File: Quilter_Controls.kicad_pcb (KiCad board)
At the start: 2 copper layers, 50.6 x 110 mm, 16 parts, among them J1 Conn_01x10_Male, J10 Conn_01x04_Male, J2 Conn_01x10_Male, J3 Conn_01x10_Male, J4 Audio_In, J5 Audio_Out, J6 Audio_Mix, J7 Freq_V_Oct, J8 Freq_CV, J9 Conn_02x04_Top_Bottom

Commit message: First draft routing of Controls PCB
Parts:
- J1, J2: moved to B.Cu
- moved TP1 91.0 mm to (53.7, 55.5)
- moved TP3 80.7 mm to (70.2, 43.0)
- moved J9 72.7 mm to (60.6, 43.8), turned to -90 degrees
- moved TP4 64.7 mm to (86.9, 147.0)
- moved TP2 62.9 mm to (86.6, 55.5)
- moved J10 40.9 mm to (87.8, 43.7), turned to -90 degrees
- moved J8 14.2 mm to (80.0, 100.9)
- moved J5 13.5 mm to (80.0, 121.3)
- moved J1 11.4 mm to (87.9, 62.8), turned to 180 degrees
- moved J7 10.1 mm to (60.4, 100.9)
- moved J6 9.27 mm to (70.2, 138.9), turned to 180 degrees
- moved J4 9.12 mm to (60.4, 121.3)
- moved J3 8.88 mm to (81.7, 147.9)
- moved Q_CTRL1 7.91 mm to (70.2, 79.2)
- moved FREQ_POT1 7.91 mm to (70.2, 55.5)
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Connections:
- J1 pad 1: unconnected-(J1-Pad1) -> -12V
- J1 pad 3: unconnected-(J1-Pad3) -> /AUDIO_BUFF3
- J1 pad 7: unconnected-(J1-Pad7) -> /FREQ_V_OCT2
- J1 pad 8: /AUDIO_BUFF4 -> unconnected-(J1-Pad8)
- J2 pad 1: unconnected-(J2-Pad1) -> +12V
- J2 pad 10: /FREQ_POT_5V -> /AUDIO_IN2
- J2 pad 2: /AUDIO_BUFF3 -> unconnected-(J2-Pad2)
- J2 pad 4: /FREQ_V_OCT2 -> unconnected-(J2-Pad4)
- J2 pad 5: unconnected-(J2-Pad5) -> /AUDIO_BUFF4
- J2 pad 7: unconnected-(J2-Pad7) -> /FREQ_POT_5V
- J2 pad 9: /AUDIO_IN2 -> unconnected-(J2-Pad9)
- J3 pad 1: unconnected-(J3-Pad1) -> /AUDIO_IN4
- J3 pad 3: /FREQ_CV4 -> unconnected-(J3-Pad3)
- J3 pad 5: /AUDIO_IN4 -> /FREQ_POT
- J3 pad 6: /FREQ_CV1 -> /FREQ_CV4
- J3 pad 7: /FREQ_POT -> /FREQ_CV1
- J9 pad 2: /AUDIO_IN2 -> /FREQ_V_OCT1
- J9 pad 3: /AUDIO_IN3 -> /AUDIO_IN2
- J9 pad 4: /AUDIO_IN4 -> /FREQ_V_OCT2
- J9 pad 5: /FREQ_V_OCT1 -> /AUDIO_IN3
- J9 pad 6: /FREQ_V_OCT2 -> /FREQ_V_OCT3
- J9 pad 7: /FREQ_V_OCT3 -> /AUDIO_IN4
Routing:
- net /AUDIO_IN4: track 0.00 -> 156.8 mm
- net /FREQ_V_OCT3: track 0.00 -> 142.3 mm
- net /FREQ_V_OCT4: track 0.00 -> 126.1 mm
- net /AUDIO_IN3: track 0.00 -> 125.1 mm
- net /AUDIO_BUFF2: track 0.00 -> 115.0 mm
- net /AUDIO_IN1: track 0.00 -> 112.0 mm, vias 0 -> 1
- net /FREQ_POT: track 0.00 -> 111.0 mm, vias 0 -> 1
- net /FREQ_V_OCT2: track 0.00 -> 109.0 mm
- net /FREQ_V_OCT1: track 0.00 -> 108.9 mm
- net /AUDIO_BUFF4: track 0.00 -> 100.2 mm
- net /AUDIO_BUFF1: track 0.00 -> 92.3 mm
- net /AUDIO_MIX: track 0.00 -> 91.3 mm
- net /Q_POT: track 0.00 -> 82.2 mm, vias 0 -> 1
- net /AUDIO_BUFF3: track 0.00 -> 81.8 mm
- net /AUDIO_IN2: track 0.00 -> 79.6 mm
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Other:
- board size 50.6 x 110 mm -> 40.4 x 110 mm

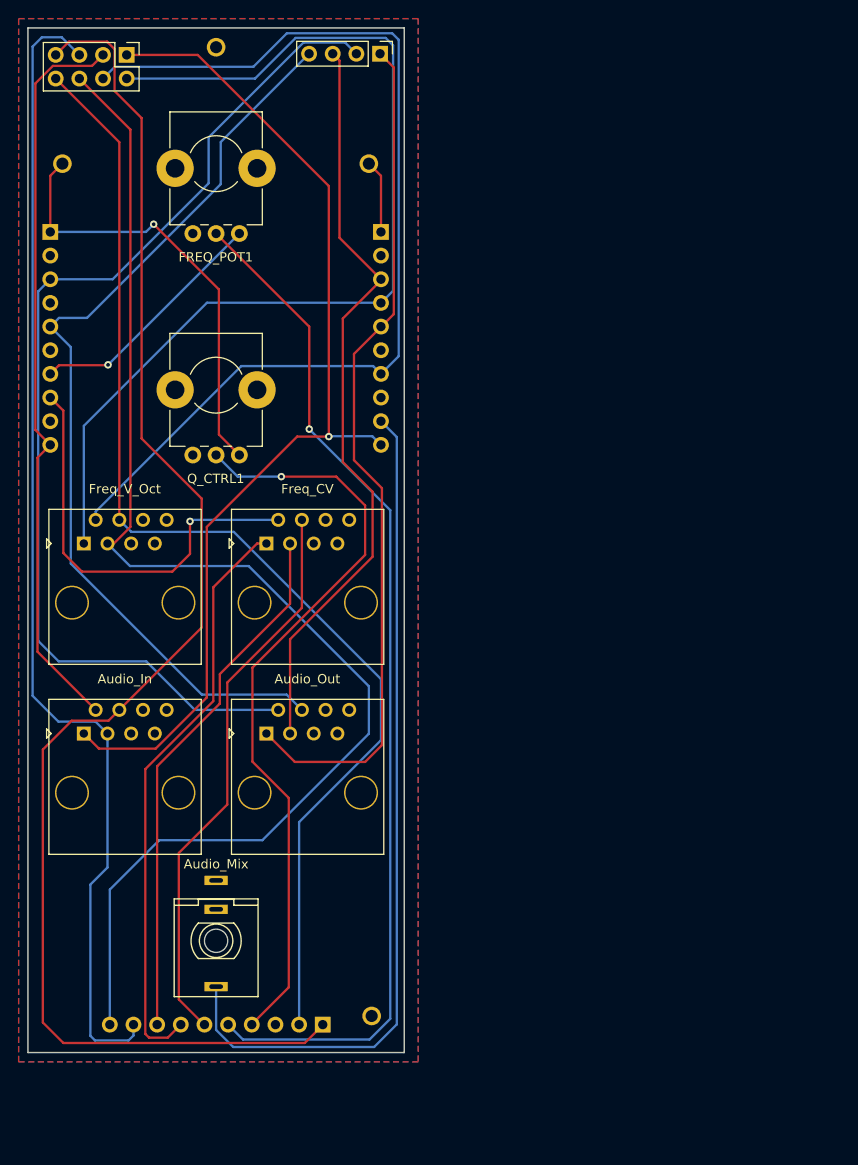
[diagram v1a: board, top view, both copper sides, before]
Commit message: Fixed orientation of connector headers
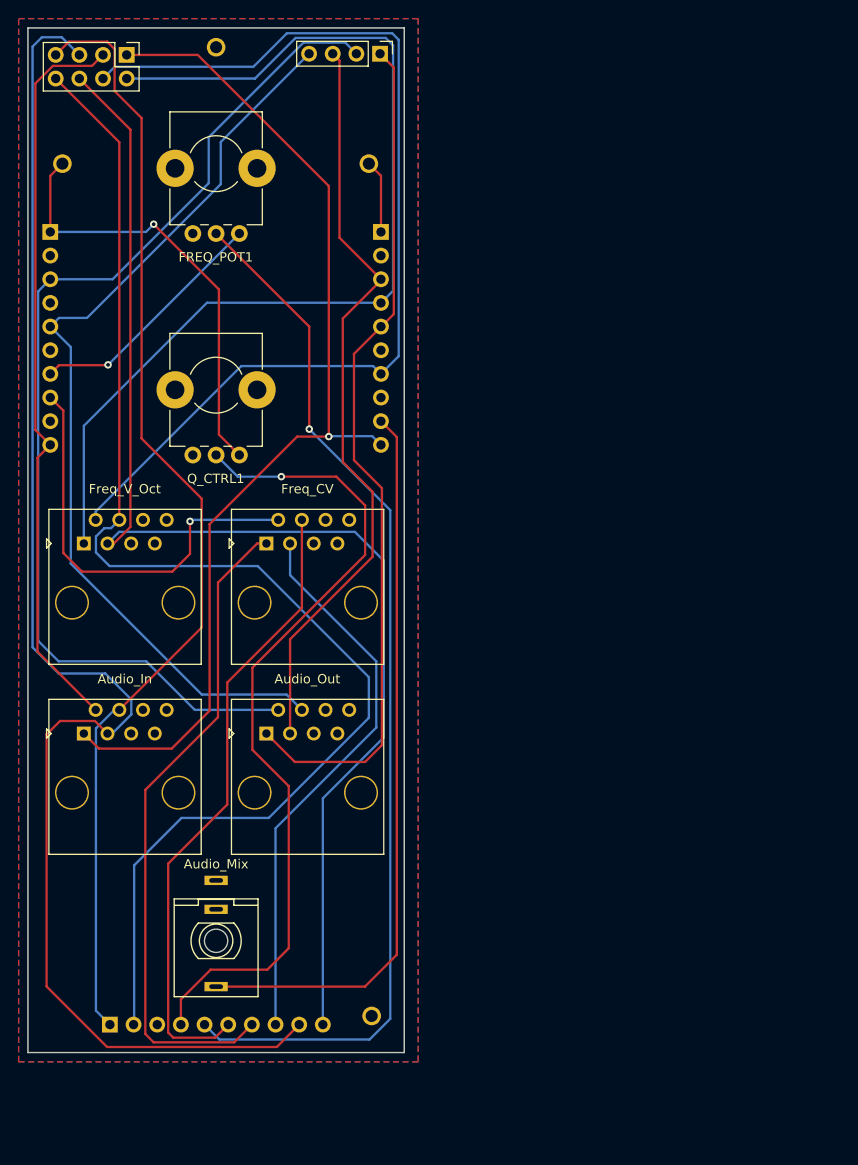
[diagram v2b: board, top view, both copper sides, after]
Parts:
- moved J3 22.9 mm to (58.8, 147.9), turned to -90 degrees
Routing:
- net /AUDIO_IN4: track 156.8 -> 121.5 mm
- net /AUDIO_IN3: track 125.1 -> 154.2 mm
- net /FREQ_V_OCT4: track 126.1 -> 143.3 mm
- net /AUDIO_MIX: track 91.3 -> 78.8 mm
- net /FREQ_CV1: track 63.2 -> 71.2 mm
- net /FREQ_CV4: track 60.8 -> 68.2 mm
- net /Q_POT: track 82.2 -> 89.0 mm
- net /FREQ_V_OCT3: track 142.3 -> 137.6 mm
- net /FREQ_POT: track 111.0 -> 113.6 mm
- net /FREQ_CV3: track 57.6 -> 60.0 mm
- net /AUDIO_IN1: track 112.0 -> 113.0 mm
